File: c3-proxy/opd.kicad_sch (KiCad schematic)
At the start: 10 parts, among them U2 INA226

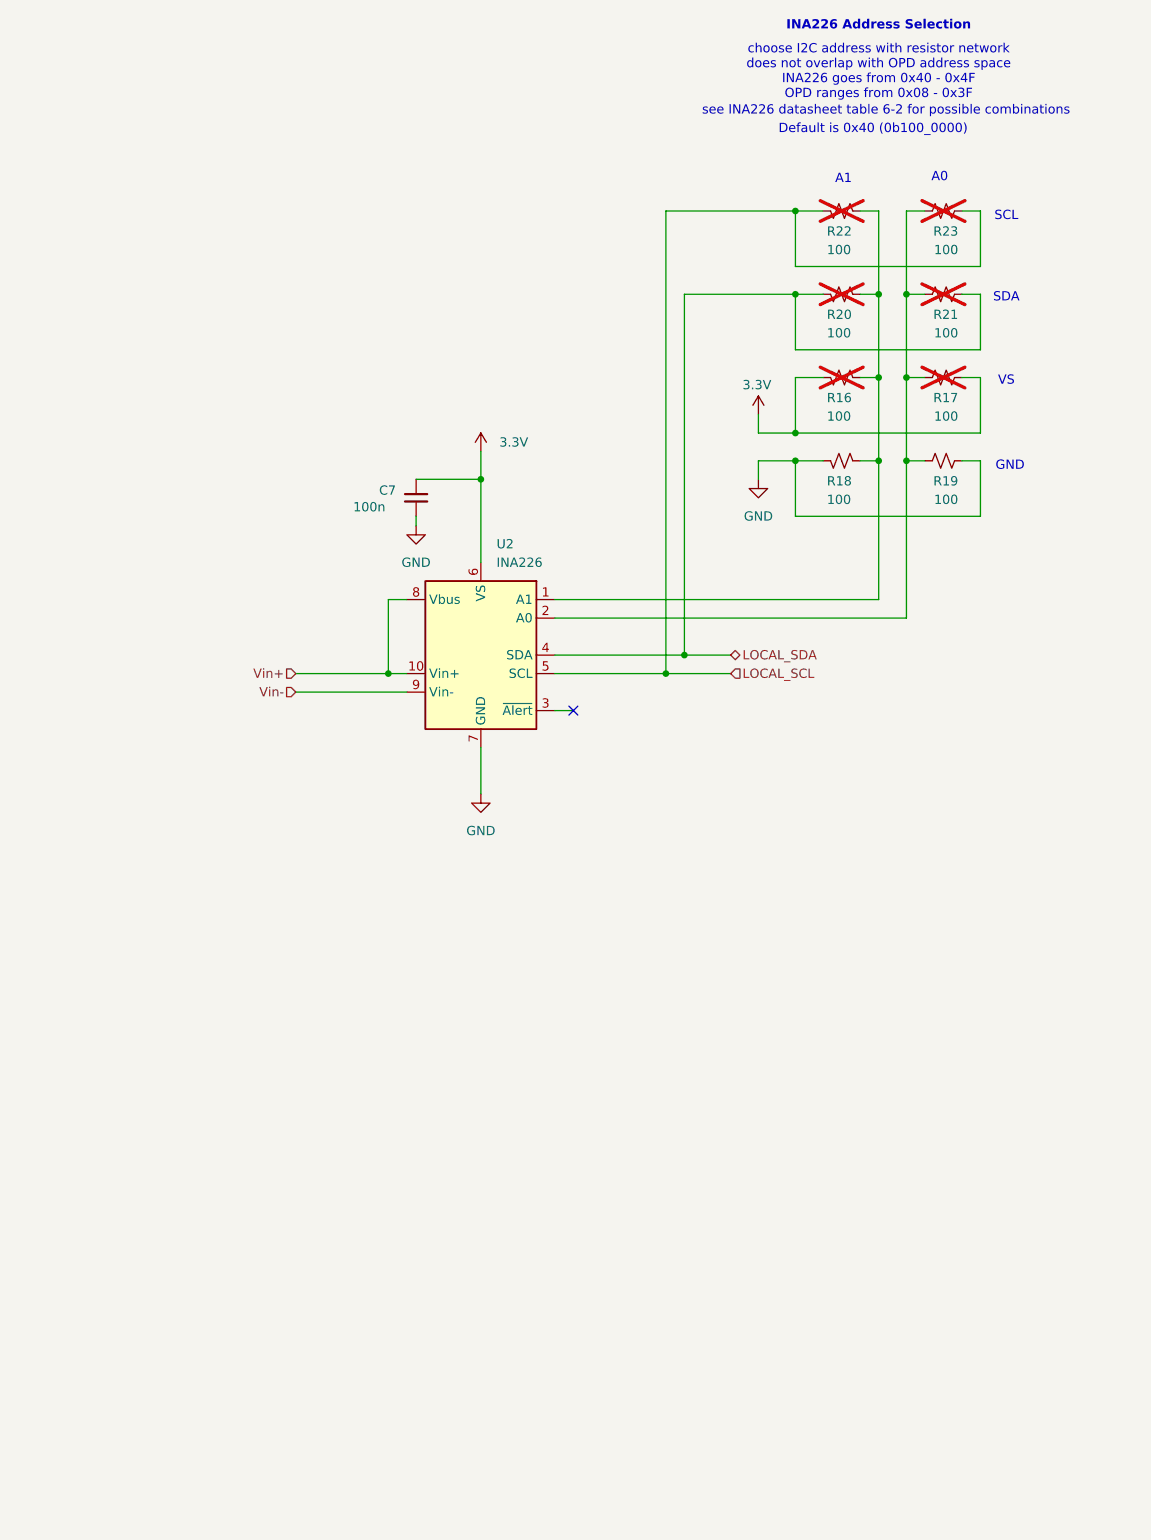
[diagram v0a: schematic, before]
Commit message: Final tweaks on v1.1.
Added more LEDs for main power, polished high power connections, DRC, ERC, etc. Added release folder.
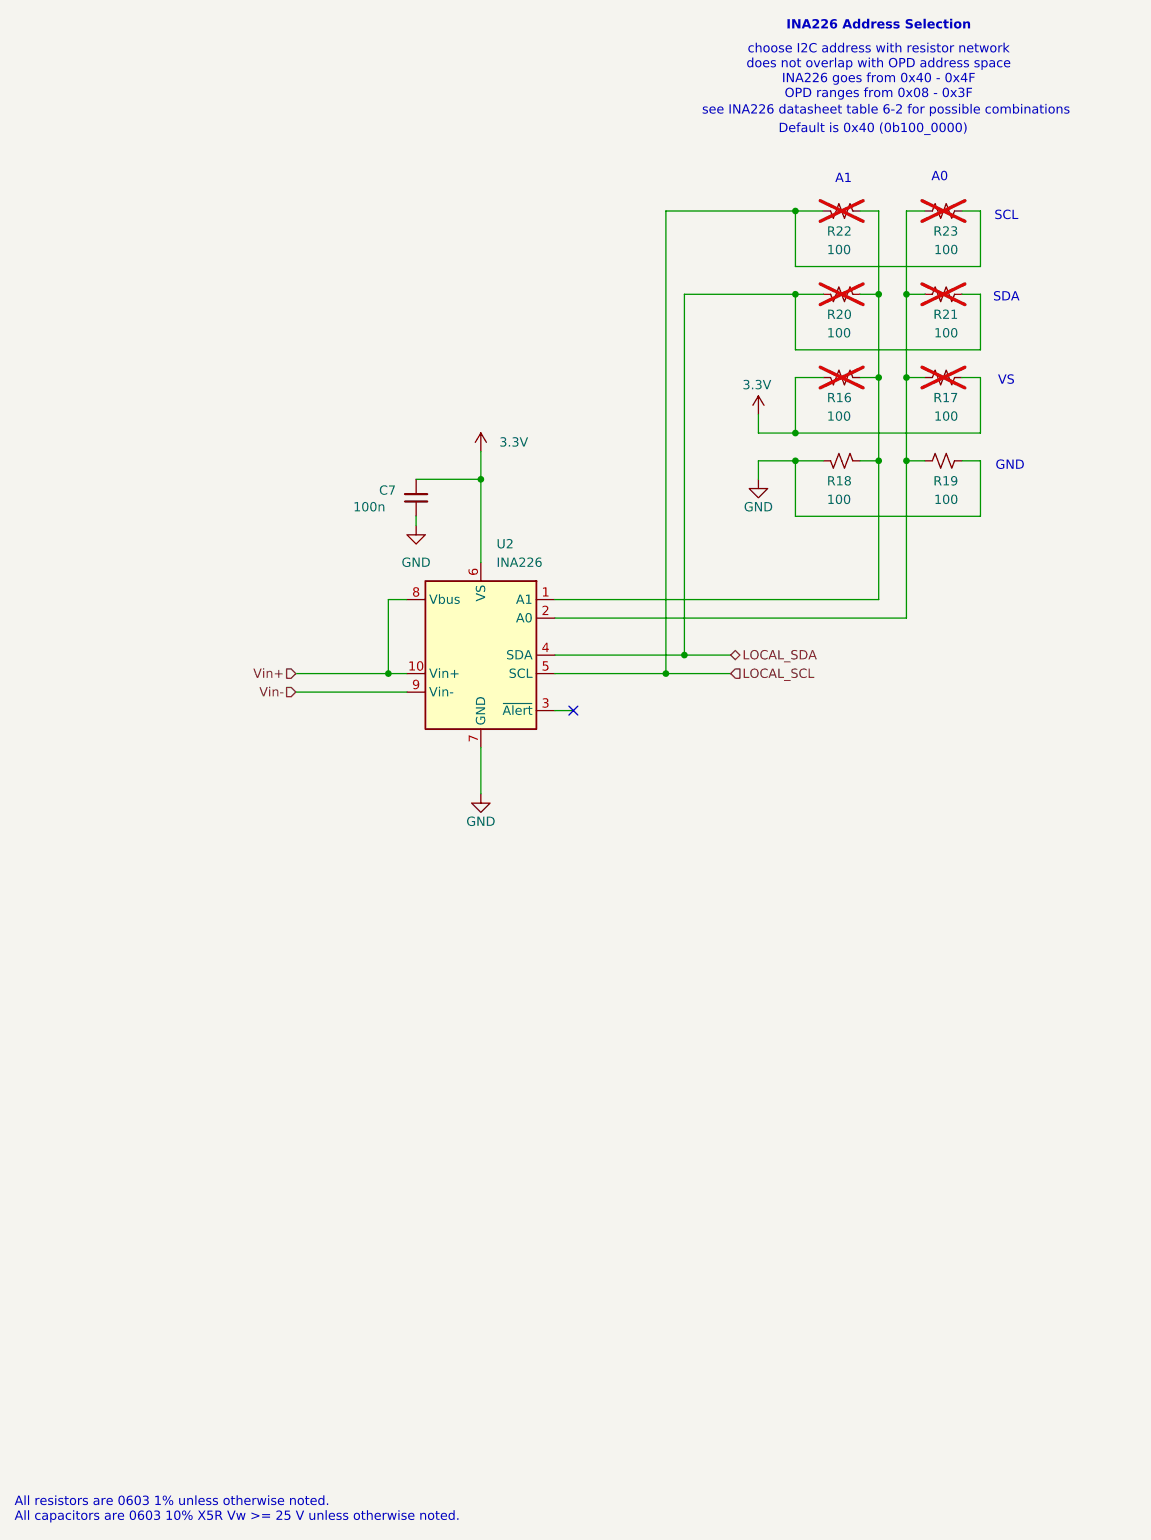
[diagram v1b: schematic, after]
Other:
- note added: "All resistors are 0603 1% unless otherwise noted. All capacitors are 0603 10% X5R Vw >= 25 V unless otherwise noted."
- title: c3-Proxy card -> c3-Proxy Board
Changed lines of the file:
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@@
 	(paper "B")
 	(title_block
-		(title "c3-Proxy card")
-		(date "2026-09-07")
-		(rev "${REVISION}")
+		(title "c3-Proxy Board")
+		(date "2026-09-08")
+		(rev "1.1")
 		(company "Portland State Aerospace Society")
 	)
@@
 				(bold yes)
 			)
+		)
+	)
+	(text "All resistors are 0603 1% unless otherwise noted.\nAll capacitors are 0603 10% X5R Vw >= 25 V unless otherwise noted."
+		(exclude_from_sim no)
+		(at 113.792 264.668 0)
+		(effects
+			(font
+				(size 1.27 1.27)
+			)
+			(justify left)
 		)
 	)
@@
 		(in_pos_files yes)
 		(dnp no)
-		(fields_autoplaced yes)
 		(property "Reference" "#PWR09"
 			(at 177.8 172.72 0)
@@
 		)
 		(property "Value" "GND"
-			(at 177.8 171.45 0)
+			(at 177.8 170.18 0)
 			(show_name no)
 			(do_not_autoplace no)
@@
 		(in_pos_files yes)
 		(dnp no)
-		(fields_autoplaced yes)
 		(property "Reference" "#PWR020"
 			(at 215.9 129.54 0)
@@
 		)
 		(property "Value" "GND"
-			(at 215.9 128.27 0)
-			(show_name no)
-			(do_not_autoplace no)
+			(at 215.9 127 0)
+			(show_name no)
+			(do_not_autoplace no)
